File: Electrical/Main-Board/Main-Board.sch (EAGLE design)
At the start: 4 parts, among them IC1 ATMEGA16A-PU, J1 FTSH-105-01-L-DV-K-A-P-TR

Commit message: Updated schematic
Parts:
- added R2, R3: 10K/10%, rcl:R-EU_R0603
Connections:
- new net LCD-DB0: IC1.PA0_[ADC0]
- new net LCD-DB1: IC1.PA1_[ADC1]
- new net LCD-DB2: IC1.PA2_[ADC2]
- new net LCD-DB3: IC1.PA3_[ADC3]
- new net LCD-DB4: IC1.PA4_[ADC4]
- new net LCD-DB5: IC1.PA5_[ADC5]
- new net LCD-DB6: IC1.PA6_[ADC6]
- new net LCD-DB7: IC1.PA7_[ADC7]
- new net SCL: IC1.PC0_[SCL], R3.1
- new net SDA: IC1.PC1_[SDA], R2.1
- net +5V/1: now also R2.2, R3.2
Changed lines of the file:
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@@
 <part name="S1" library="SamacSys_Parts" deviceset="PTS647SM50SMTR2LFS" device=""/>
 <part name="R1" library="rcl" library_urn="urn:adsk.eagle:library:334" deviceset="R-EU_" device="R0603" package3d_urn="urn:adsk.eagle:package:23555/3" value="10K/10%"/>
+<part name="R2" library="rcl" library_urn="urn:adsk.eagle:library:334" deviceset="R-EU_" device="R0603" package3d_urn="urn:adsk.eagle:package:23555/3" value="10K/10%"/>
+<part name="R3" library="rcl" library_urn="urn:adsk.eagle:library:334" deviceset="R-EU_" device="R0603" package3d_urn="urn:adsk.eagle:package:23555/3" value="10K/10%"/>
 </parts>
 <sheets>
@@
 <attribute name="VALUE" x="149.86" y="91.44" size="1.778" layer="96"/>
 </instance>
-<instance part="GND2" gate="1" x="220.98" y="93.98" smashed="yes">
-<attribute name="VALUE" x="218.44" y="91.44" size="1.778" layer="96"/>
-</instance>
-<instance part="SUPPLY1" gate="G$1" x="215.9" y="193.04" smashed="yes">
-<attribute name="VALUE" x="212.725" y="196.215" size="1.778" layer="96"/>
+<instance part="GND2" gate="1" x="233.68" y="93.98" smashed="yes">
+<attribute name="VALUE" x="231.14" y="91.44" size="1.778" layer="96"/>
+</instance>
+<instance part="SUPPLY1" gate="G$1" x="226.06" y="193.04" smashed="yes">
+<attribute name="VALUE" x="222.885" y="196.215" size="1.778" layer="96"/>
 </instance>
 <instance part="SUPPLY2" gate="G$1" x="152.4" y="193.04" smashed="yes">
@@
 <attribute name="NAME" x="140.97" y="164.0586" size="1.778" layer="95"/>
 <attribute name="VALUE" x="140.97" y="161.798" size="1.778" layer="96"/>
+</instance>
+<instance part="R2" gate="G$1" x="220.98" y="139.7" smashed="yes" rot="R90">
+<attribute name="NAME" x="222.25" y="141.1986" size="1.778" layer="95"/>
+<attribute name="VALUE" x="222.25" y="138.938" size="1.778" layer="96"/>
+</instance>
+<instance part="R3" gate="G$1" x="226.06" y="139.7" smashed="yes" rot="R90">
+<attribute name="NAME" x="227.33" y="141.1986" size="1.778" layer="95"/>
+<attribute name="VALUE" x="227.33" y="138.938" size="1.778" layer="96"/>
 </instance>
 </instances>
@@
 <pinref part="IC1" gate="G$1" pin="GND_1"/>
 <pinref part="GND2" gate="1" pin="GND"/>
-<wire x1="210.82" y1="152.4" x2="220.98" y2="152.4" width="0.1524" layer="91"/>
-<wire x1="220.98" y1="152.4" x2="220.98" y2="96.52" width="0.1524" layer="91"/>
+<wire x1="210.82" y1="152.4" x2="233.68" y2="152.4" width="0.1524" layer="91"/>
+<wire x1="233.68" y1="152.4" x2="233.68" y2="96.52" width="0.1524" layer="91"/>
 </segment>
 <segment>
@@
 <segment>
 <pinref part="IC1" gate="G$1" pin="AVCC"/>
-<wire x1="210.82" y1="149.86" x2="215.9" y2="149.86" width="0.1524" layer="91"/>
-<wire x1="215.9" y1="149.86" x2="215.9" y2="154.94" width="0.1524" layer="91"/>
+<wire x1="210.82" y1="149.86" x2="220.98" y2="149.86" width="0.1524" layer="91"/>
+<wire x1="220.98" y1="149.86" x2="226.06" y2="149.86" width="0.1524" layer="91"/>
+<wire x1="226.06" y1="149.86" x2="226.06" y2="154.94" width="0.1524" layer="91"/>
 <pinref part="IC1" gate="G$1" pin="AREF"/>
-<wire x1="215.9" y1="154.94" x2="210.82" y2="154.94" width="0.1524" layer="91"/>
-<wire x1="215.9" y1="154.94" x2="215.9" y2="190.5" width="0.1524" layer="91"/>
-<junction x="215.9" y="154.94"/>
+<wire x1="226.06" y1="154.94" x2="210.82" y2="154.94" width="0.1524" layer="91"/>
+<wire x1="226.06" y1="154.94" x2="226.06" y2="190.5" width="0.1524" layer="91"/>
+<junction x="226.06" y="154.94"/>
 <pinref part="SUPPLY1" gate="G$1" pin="+5V/1"/>
+<pinref part="R2" gate="G$1" pin="2"/>
+<wire x1="220.98" y1="144.78" x2="220.98" y2="149.86" width="0.1524" layer="91"/>
+<junction x="220.98" y="149.86"/>
+<pinref part="R3" gate="G$1" pin="2"/>
+<wire x1="226.06" y1="144.78" x2="226.06" y2="149.86" width="0.1524" layer="91"/>
+<junction x="226.06" y="149.86"/>
 </segment>
 <segment>
@@
 </segment>
 </net>
+<net name="SDA" class="0">
+<segment>
+<pinref part="IC1" gate="G$1" pin="PC1_[SDA]"/>
+<wire x1="210.82" y1="132.08" x2="220.98" y2="132.08" width="0.1524" layer="91"/>
+<label x="228.6" y="132.08" size="0.8128" layer="95" xref="yes"/>
+<pinref part="R2" gate="G$1" pin="1"/>
+<wire x1="220.98" y1="132.08" x2="228.6" y2="132.08" width="0.1524" layer="91"/>
+<wire x1="220.98" y1="134.62" x2="220.98" y2="132.08" width="0.1524" layer="91"/>
+<junction x="220.98" y="132.08"/>
+</segment>
+</net>
+<net name="SCL" class="0">
+<segment>
+<pinref part="IC1" gate="G$1" pin="PC0_[SCL]"/>
+<wire x1="210.82" y1="129.54" x2="226.06" y2="129.54" width="0.1524" layer="91"/>
+<label x="228.6" y="129.54" size="0.8128" layer="95" xref="yes"/>
+<pinref part="R3" gate="G$1" pin="1"/>
+<wire x1="226.06" y1="129.54" x2="228.6" y2="129.54" width="0.1524" layer="91"/>
+<wire x1="226.06" y1="134.62" x2="226.06" y2="129.54" width="0.1524" layer="91"/>
+<junction x="226.06" y="129.54"/>
+</segment>
+</net>
+<net name="LCD-DB0" class="0">
+<segment>
+<pinref part="IC1" gate="G$1" pin="PA0_[ADC0]"/>
+<wire x1="210.82" y1="175.26" x2="213.36" y2="175.26" width="0.1524" layer="91"/>
+<label x="213.36" y="175.26" size="0.8128" layer="95" xref="yes"/>
+</segment>
+</net>
+<net name="LCD-DB1" class="0">
+<segment>
+<pinref part="IC1" gate="G$1" pin="PA1_[ADC1]"/>
+<wire x1="210.82" y1="172.72" x2="213.36" y2="172.72" width="0.1524" layer="91"/>
+<label x="213.36" y="172.72" size="0.8128" layer="95" xref="yes"/>
+</segment>
+</net>
+<net name="LCD-DB2" class="0">
+<segment>
+<pinref part="IC1" gate="G$1" pin="PA2_[ADC2]"/>
+<wire x1="210.82" y1="170.18" x2="213.36" y2="170.18" width="0.1524" layer="91"/>
+<label x="213.36" y="170.18" size="0.8128" layer="95" xref="yes"/>
+</segment>
+</net>
+<net name="LCD-DB3" class="0">
+<segment>
+<pinref part="IC1" gate="G$1" pin="PA3_[ADC3]"/>
+<wire x1="210.82" y1="167.64" x2="213.36" y2="167.64" width="0.1524" layer="91"/>
+<label x="213.36" y="167.64" size="0.8128" layer="95" xref="yes"/>
+</segment>
+</net>
+<net name="LCD-DB4" class="0">
+<segment>
+<pinref part="IC1" gate="G$1" pin="PA4_[ADC4]"/>
+<wire x1="210.82" y1="165.1" x2="213.36" y2="165.1" width="0.1524" layer="91"/>
+<label x="213.36" y="165.1" size="0.8128" layer="95" xref="yes"/>
+</segment>
+</net>
+<net name="LCD-DB5" class="0">
+<segment>
+<pinref part="IC1" gate="G$1" pin="PA5_[ADC5]"/>
+<wire x1="210.82" y1="162.56" x2="213.36" y2="162.56" width="0.1524" layer="91"/>
+<label x="213.36" y="162.56" size="0.8128" layer="95" xref="yes"/>
+</segment>
+</net>
+<net name="LCD-DB6" class="0">
+<segment>
+<pinref part="IC1" gate="G$1" pin="PA6_[ADC6]"/>
+<wire x1="210.82" y1="160.02" x2="213.36" y2="160.02" width="0.1524" layer="91"/>
+<label x="213.36" y="160.02" size="0.8128" layer="95" xref="yes"/>
+</segment>
+</net>
+<net name="LCD-DB7" class="0">
+<segment>
+<pinref part="IC1" gate="G$1" pin="PA7_[ADC7]"/>
+<wire x1="210.82" y1="157.48" x2="213.36" y2="157.48" width="0.1524" layer="91"/>
+<label x="213.36" y="157.48" size="0.8128" layer="95" xref="yes"/>
+</segment>
+</net>

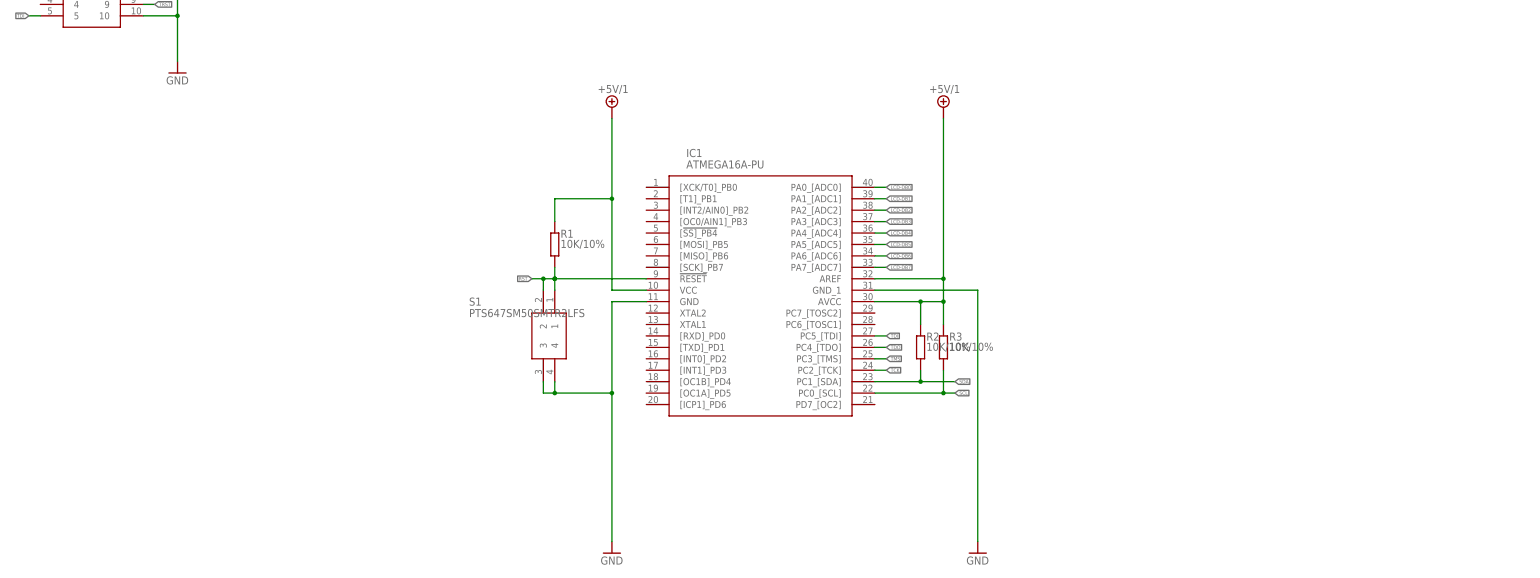
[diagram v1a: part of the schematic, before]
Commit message: Updated schematic
Added a similar LCD and µC:2
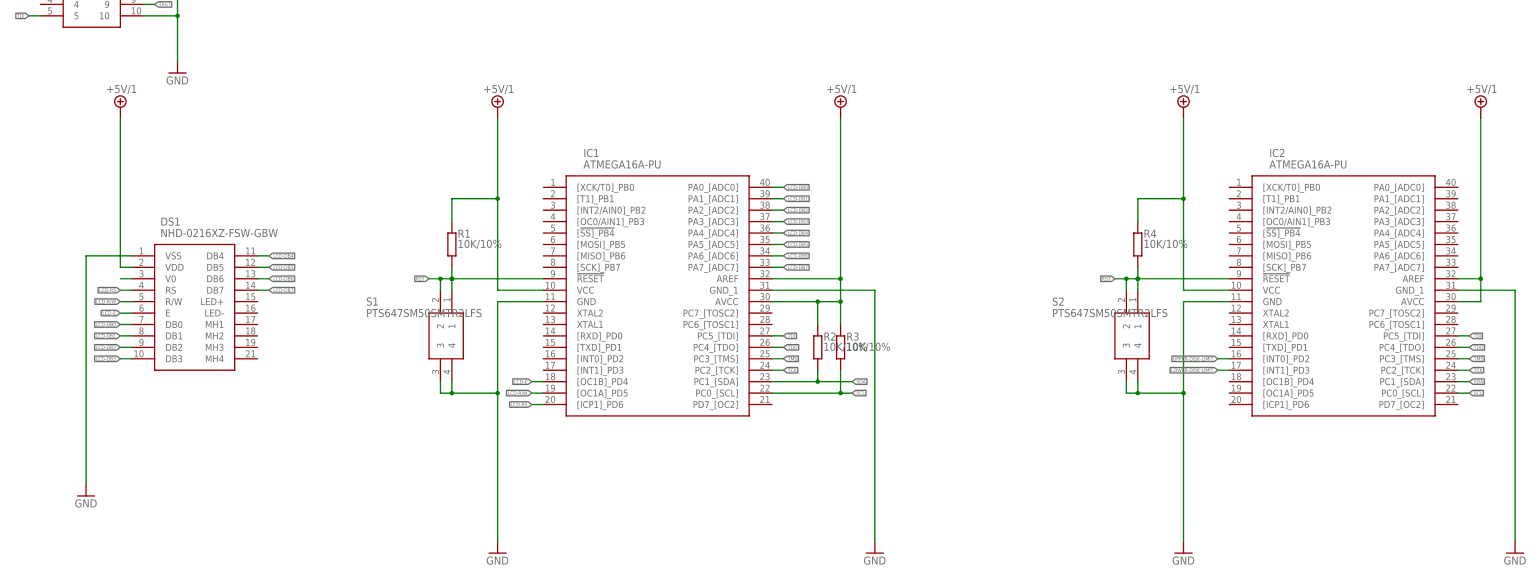
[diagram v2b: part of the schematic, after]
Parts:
- added DS1: NHD-0216XZ-FSW-GBW, SamacSys_Parts:NHD-0216XZ-FSW-GBW
- added IC2: ATMEGA16A-PU, SamacSys_Parts:ATMEGA16A-PU
- added R4: 10K/10%, rcl:R-EU_R0603
- added S2: PTS647SM50SMTR2LFS, SamacSys_Parts:PTS647SM50SMTR2LFS
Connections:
- new net LCD-E: DS1.E, IC1.[OC1B]_PD4
- new net LCD-R/W: DS1.R/W, IC1.[OC1A]_PD5
- new net LCD-RS: DS1.RS, IC1.[ICP1]_PD6
- new net LOWER-DISK-LIMIT: IC2.[INT1]_PD3
- new net N$2: DS1.V0
- new net UPPER-DISK-LIMIT: IC2.[INT0]_PD2
- net +5V/1: now also DS1.VDD, IC2.AREF, IC2.AVCC, IC2.VCC, R4.2
- net GND: now also DS1.VSS, IC2.GND, IC2.GND_1, S2.3, S2.4
- net LCD-DB0: now also DS1.DB0
- net LCD-DB1: now also DS1.DB1
- net LCD-DB2: now also DS1.DB2
- net LCD-DB3: now also DS1.DB3
- net LCD-DB4: now also DS1.DB4
- net LCD-DB5: now also DS1.DB5
- net LCD-DB6: now also DS1.DB6
- net LCD-DB7: now also DS1.DB7
- net RST: now also IC2.!RESET, R4.1, S2.1, S2.2
- net SCL: now also IC2.PC0_[SCL]
- net SDA: now also IC2.PC1_[SDA]
- net TCK: now also IC2.PC2_[TCK]
- net TDI: now also IC2.PC5_[TDI]
- net TDO: now also IC2.PC4_[TDO]
- net TMS: now also IC2.PC3_[TMS]
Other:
- moved on the sheet: IC1, R1, R2, R3, S1

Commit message: Added motor things to schematic
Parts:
- added IC3: AZ1117CH-ADJTRG1, SamacSys_Parts:AZ1117CH-ADJTRG1
- added IC4: AZ1117CH-5.0TRG1DITR-ND, SamacSys_Parts:AZ1117CH-5.0TRG1DITR-ND
- added IC5: LM2904DRG3, SamacSys_Parts:LM2904DRG3
- added J2, J3: 0022288033, 0022288033:0022288033
- added R10, R11: 10K/5%, rcl:R-EU_R0603
- added R5: 200R/5%, rcl:R-EU_R0603
- added R6: 866R/5%, rcl:R-EU_R0603
- added R7, R9: 100R/5%, rcl:R-EU_R0603
- added R8: ERJ-L1WKF10CU, SamacSys_Parts:ERJ-L1WKF10CU
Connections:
- new net +12V: IC3.INPUT, IC4.INPUT
- new net +7.5V: J2.2, J3.2, R8.R2, R9.1
- new net DABDA: IC3.OUTPUT, IC3.VOUT, R5.2, R7.1, R8.R1
- new net MOTOR_OVER-CURRENT: IC2.[INT2/AIN0]_PB2, IC5.1OUT, R10.2
- new net N$1: IC5.1IN+, R11.2, R7.2
- new net N$5: IC5.1IN-, R10.1, R9.2
- new net SERVO-LOWER: IC2.[OC1A]_PD5, J3.3
- new net SERVO-UPPER: IC2.[OC1B]_PD4, J2.3
- new net W3R355: IC3.ADJ/GND, R5.1, R6.2
- net +5V/1: now also IC4.OUTPUT, IC4.VOUT_TAB, IC5.VCC
- net GND: now also IC4.ADJ/GND, IC5.GND, J2.1, J3.1, R11.1, R6.1
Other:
- note added: "JaG HetER BoB"

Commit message: Did some layout
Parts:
- added J4: PJ-031DH, SamacSys_Parts:PJ-031DH
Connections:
- net +12V: now also J4.SLEEVE
- net GND: now also J4.TIP
- net LCD-E: now also IC1.[INT2/AIN0]_PB2; no longer IC1.[OC1B]_PD4
- net LCD-R/W: now also IC1.[T1]_PB1; no longer IC1.[OC1A]_PD5
- net LCD-RS: now also IC1.[XCK/T0]_PB0; no longer IC1.[ICP1]_PD6
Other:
- moved on the sheet: IC4, J2, J3

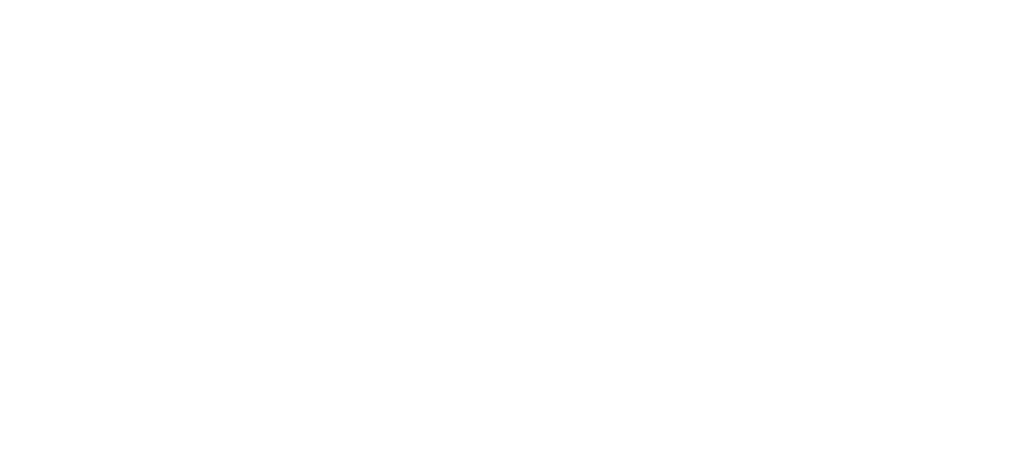
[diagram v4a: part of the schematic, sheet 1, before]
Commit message: Updated layout
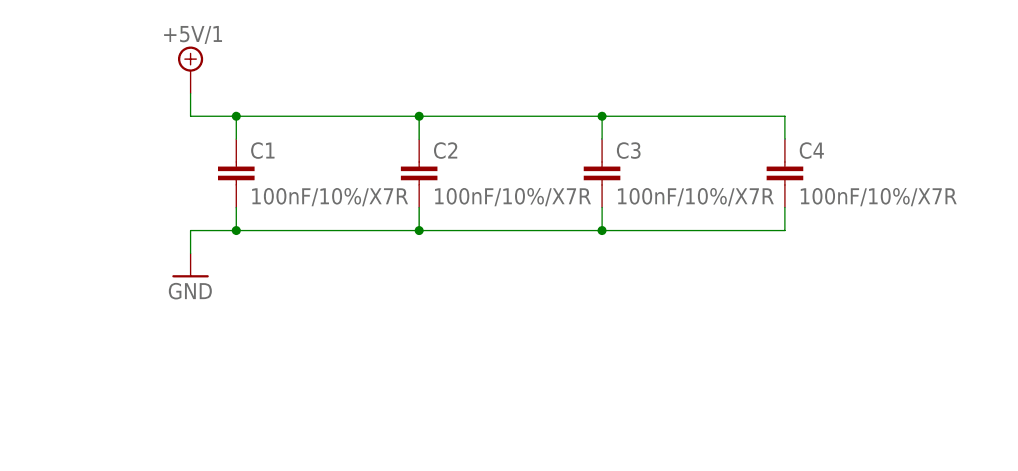
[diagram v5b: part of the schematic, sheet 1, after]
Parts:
- added C1, C2, C3, C4: 100nF/10%/X7R, rcl:C-EUC0603
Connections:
- net +5V/1: now also C1.1, C2.1, C3.1, C4.1
- net GND: now also C1.2, C2.2, C3.2, C4.2
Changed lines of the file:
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@@
 <part name="SUPPLY11" library="supply2" library_urn="urn:adsk.eagle:library:372" deviceset="+12V" device=""/>
 <part name="GND12" library="supply1" library_urn="urn:adsk.eagle:library:371" deviceset="GND" device=""/>
+<part name="C1" library="rcl" library_urn="urn:adsk.eagle:library:334" deviceset="C-EU" device="C0603" package3d_urn="urn:adsk.eagle:package:23616/2" value="100nF/10%/X7R"/>
+<part name="C2" library="rcl" library_urn="urn:adsk.eagle:library:334" deviceset="C-EU" device="C0603" package3d_urn="urn:adsk.eagle:package:23616/2" value="100nF/10%/X7R"/>
+<part name="C3" library="rcl" library_urn="urn:adsk.eagle:library:334" deviceset="C-EU" device="C0603" package3d_urn="urn:adsk.eagle:package:23616/2" value="100nF/10%/X7R"/>
+<part name="C4" library="rcl" library_urn="urn:adsk.eagle:library:334" deviceset="C-EU" device="C0603" package3d_urn="urn:adsk.eagle:package:23616/2" value="100nF/10%/X7R"/>
+<part name="SUPPLY12" library="supply2" library_urn="urn:adsk.eagle:library:372" deviceset="+5V/1" device=""/>
+<part name="GND13" library="supply1" library_urn="urn:adsk.eagle:library:371" deviceset="GND" device=""/>
 </parts>
 <sheets>
@@
 <attribute name="VALUE" x="53.34" y="33.02" size="1.778" layer="96"/>
 </instance>
+<instance part="C1" gate="G$1" x="292.1" y="238.76" smashed="yes">
+<attribute name="NAME" x="293.624" y="239.141" size="1.778" layer="95"/>
+<attribute name="VALUE" x="293.624" y="234.061" size="1.778" layer="96"/>
+</instance>
+<instance part="C2" gate="G$1" x="312.42" y="238.76" smashed="yes">
+<attribute name="NAME" x="313.944" y="239.141" size="1.778" layer="95"/>
+<attribute name="VALUE" x="313.944" y="234.061" size="1.778" layer="96"/>
+</instance>
+<instance part="C3" gate="G$1" x="332.74" y="238.76" smashed="yes">
+<attribute name="NAME" x="334.264" y="239.141" size="1.778" layer="95"/>
+<attribute name="VALUE" x="334.264" y="234.061" size="1.778" layer="96"/>
+</instance>
+<instance part="C4" gate="G$1" x="353.06" y="238.76" smashed="yes">
+<attribute name="NAME" x="354.584" y="239.141" size="1.778" layer="95"/>
+<attribute name="VALUE" x="354.584" y="234.061" size="1.778" layer="96"/>
+</instance>
+<instance part="SUPPLY12" gate="G$1" x="287.02" y="248.92" smashed="yes">
+<attribute name="VALUE" x="283.845" y="252.095" size="1.778" layer="96"/>
+</instance>
+<instance part="GND13" gate="1" x="287.02" y="226.06" smashed="yes">
+<attribute name="VALUE" x="284.48" y="223.52" size="1.778" layer="96"/>
+</instance>
 </instances>
 <busses>
@@
 <pinref part="J4" gate="G$1" pin="TIP"/>
 <wire x1="53.34" y1="55.88" x2="55.88" y2="55.88" width="0.1524" layer="91"/>
+</segment>
+<segment>
+<pinref part="C1" gate="G$1" pin="2"/>
+<wire x1="292.1" y1="233.68" x2="292.1" y2="231.14" width="0.1524" layer="91"/>
+<wire x1="292.1" y1="231.14" x2="312.42" y2="231.14" width="0.1524" layer="91"/>
+<pinref part="C2" gate="G$1" pin="2"/>
+<wire x1="312.42" y1="231.14" x2="312.42" y2="233.68" width="0.1524" layer="91"/>
+<wire x1="312.42" y1="231.14" x2="332.74" y2="231.14" width="0.1524" layer="91"/>
+<junction x="312.42" y="231.14"/>
+<pinref part="C3" gate="G$1" pin="2"/>
+<wire x1="332.74" y1="231.14" x2="332.74" y2="233.68" width="0.1524" layer="91"/>
+<wire x1="332.74" y1="231.14" x2="353.06" y2="231.14" width="0.1524" layer="91"/>
+<junction x="332.74" y="231.14"/>
+<pinref part="C4" gate="G$1" pin="2"/>
+<wire x1="353.06" y1="231.14" x2="353.06" y2="233.68" width="0.1524" layer="91"/>
+<pinref part="GND13" gate="1" pin="GND"/>
+<wire x1="292.1" y1="231.14" x2="287.02" y2="231.14" width="0.1524" layer="91"/>
+<wire x1="287.02" y1="231.14" x2="287.02" y2="228.6" width="0.1524" layer="91"/>
+<junction x="292.1" y="231.14"/>
 </segment>
 </net>
@@
 <pinref part="SUPPLY9" gate="G$1" pin="+5V/1"/>
 </segment>
+<segment>
+<pinref part="C1" gate="G$1" pin="1"/>
+<wire x1="292.1" y1="241.3" x2="292.1" y2="243.84" width="0.1524" layer="91"/>
+<pinref part="C2" gate="G$1" pin="1"/>
+<wire x1="292.1" y1="243.84" x2="312.42" y2="243.84" width="0.1524" layer="91"/>
+<wire x1="312.42" y1="243.84" x2="312.42" y2="241.3" width="0.1524" layer="91"/>
+<wire x1="312.42" y1="243.84" x2="332.74" y2="243.84" width="0.1524" layer="91"/>
+<junction x="312.42" y="243.84"/>
+<pinref part="C3" gate="G$1" pin="1"/>
+<wire x1="332.74" y1="243.84" x2="332.74" y2="241.3" width="0.1524" layer="91"/>
+<wire x1="332.74" y1="243.84" x2="353.06" y2="243.84" width="0.1524" layer="91"/>
+<junction x="332.74" y="243.84"/>
+<pinref part="C4" gate="G$1" pin="1"/>
+<wire x1="353.06" y1="243.84" x2="353.06" y2="241.3" width="0.1524" layer="91"/>
+<wire x1="292.1" y1="243.84" x2="287.02" y2="243.84" width="0.1524" layer="91"/>
+<junction x="292.1" y="243.84"/>
+<pinref part="SUPPLY12" gate="G$1" pin="+5V/1"/>
+<wire x1="287.02" y1="243.84" x2="287.02" y2="246.38" width="0.1524" layer="91"/>
+</segment>
 </net>

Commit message: Updated schematci for more componenets
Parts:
- added C5, C6: 100nF/10%/X7R, rcl:C-EUC0603
- added C7: EEEFK1J220P, SamacSys_Parts:EEEFK1J220P
- added IC10, IC6, IC7, IC8, IC9: TLE4966L, SamacSys_Parts:TLE4966L
- added R12, R13, R14, R15, R16: 1.2K/5%, rcl:R-EU_R0603
- added VR1: EVM3YSX50B54, SamacSys_Parts:EVM3YSX50B54
- R7, R9: value 100R/5% -> 500R/5%
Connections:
- net +12V: now also C7.+
- net +5V/1: now also C5.1, C6.1, VR1.A
- net GND: now also C5.2, C6.2, C7.-, VR1.C
- net MOTOR_OVER-CURRENT: now also IC2.PA0_[ADC0]; no longer IC2.[INT2/AIN0]_PB2
- net N$2: now also VR1.B
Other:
- moved on the sheet: C1, C2, C3, C4
